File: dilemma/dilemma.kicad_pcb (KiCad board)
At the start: 2 copper layers, 142.3 x 95.1 mm, 72 parts, among them J1 S3B-PH-SM4-TB(LF)(SN), J2 Serial, J5 S3B-PH-SM4-TB(LF)(SN), SW1 SW_Push, SW10 SW_Push, SW11 SW_Push, SW12 SW_Push, SW13 SW_Push, SW14 SW_Push, SW15 SW_Push, SW16 SW_Push, SW17 SW_Push, SW2 SW_Push, SW26 SW_SPST, SW3 SW_Push, SW37 SW_SPST, SW4 SW_Push, SW5 SW_Push, SW6 SW_Push, SW7 SW_Push, SW8 SW_Push, SW9 SW_Push, U2 eliteC

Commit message: silkscreen
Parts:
- added G***: LOGO, LOGO, F.Cu at (140.1, 27.9)
- added G***: LOGO, LOGO, B.Cu at (140.1, 27.9)
- moved H1 11.8 mm to (131.1, 28.1)
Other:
- outline, holes or cut-outs redrawn

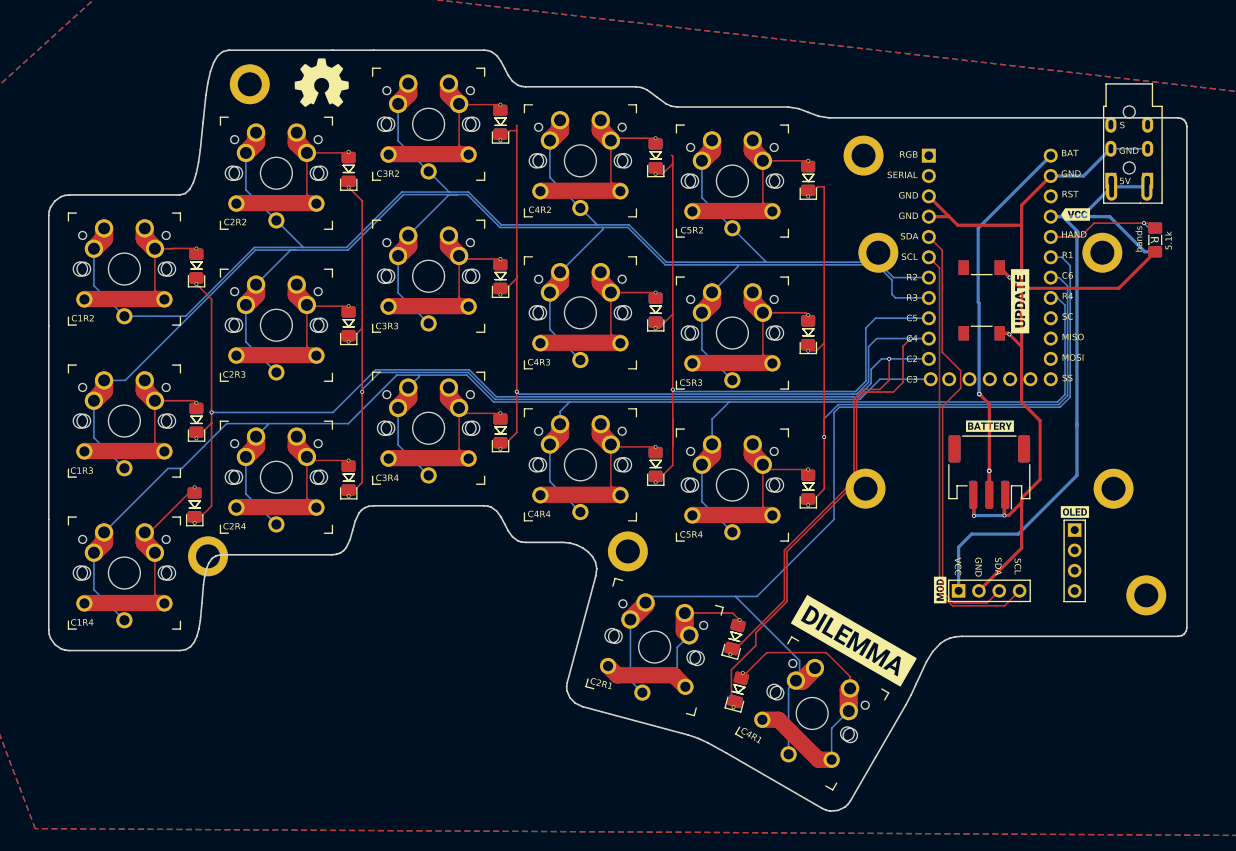
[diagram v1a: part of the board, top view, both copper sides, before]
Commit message: trackpad connector reversible
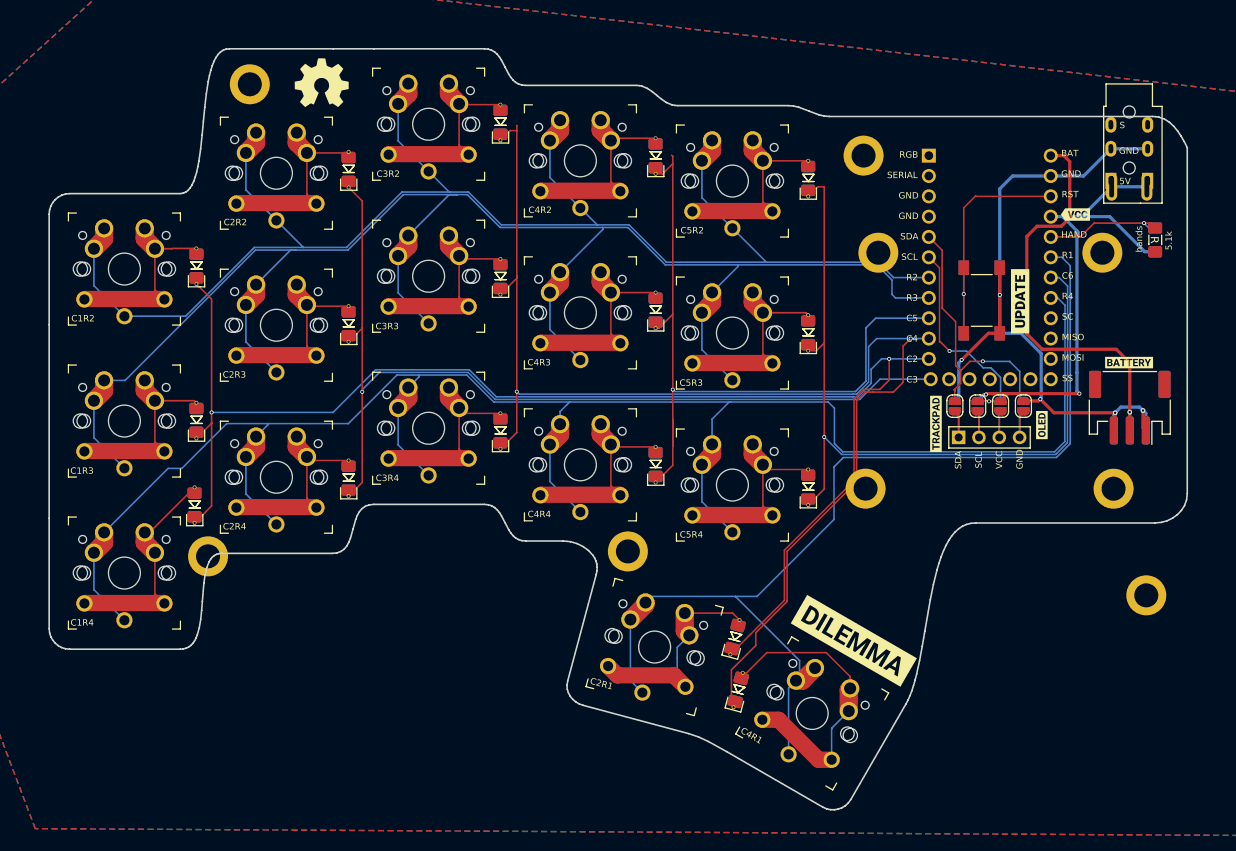
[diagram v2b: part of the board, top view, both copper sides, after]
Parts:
- removed O3: trackpad, footprints:PinHeader_1x04_P2.54mm_Vertical
- removed kibuzzard-628D3A32 (x2): G***, kibuzzard-628D3A32
- added JP1: Jumper_2_Open, footprints:SolderJumper-2_P1.3mm_Open_RoundedPad1.0x1.5mm, F.Cu at (219.2, 68.3)
- added JP2: Jumper_2_Open, footprints:SolderJumper-2_P1.3mm_Open_RoundedPad1.0x1.5mm, B.Cu at (227.8, 68.3)
- added JP3: Jumper_2_Open, footprints:SolderJumper-2_P1.3mm_Open_RoundedPad1.0x1.5mm, F.Cu at (222.1, 68.3)
- added JP4: Jumper_2_Open, footprints:SolderJumper-2_P1.3mm_Open_RoundedPad1.0x1.5mm, B.Cu at (224.9, 68.3)
- added JP5: Jumper_2_Open, footprints:SolderJumper-2_P1.3mm_Open_RoundedPad1.0x1.5mm, F.Cu at (224.9, 68.3)
- added JP6: Jumper_2_Open, footprints:SolderJumper-2_P1.3mm_Open_RoundedPad1.0x1.5mm, B.Cu at (222.1, 68.3)
- added JP7: Jumper_2_Open, footprints:SolderJumper-2_P1.3mm_Open_RoundedPad1.0x1.5mm, F.Cu at (227.8, 68.3)
- added JP8: Jumper_2_Open, footprints:SolderJumper-2_P1.3mm_Open_RoundedPad1.0x1.5mm, B.Cu at (219.2, 68.3)
- added kibuzzard-628E0199: G***, kibuzzard-628E0199, F.Cu at (216.9, 70.5)
- added kibuzzard-628E0199: G***, kibuzzard-628E0199, B.Cu at (216.9, 70.5)
- moved J5 19.3 mm to (241.1, 68.5)
- moved J1 19.3 mm to (241.1, 68.5)
- moved kibuzzard-628DFB5F 19.1 mm to (241.0, 62.9) (x2)
- moved O2 18.6 mm to (219.7, 72.2), turned to 90 degrees
- moved kibuzzard-628DFB48 11.6 mm to (230.1, 70.7), turned to -90 degrees
- moved kibuzzard-628DFB48 11.6 mm to (230.1, 70.7), turned to 90 degrees
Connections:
- O2 pad 1: sda_l -> Net-(O2-Pad1)
- O2 pad 2: scl_l -> Net-(O2-Pad2)
- O2 pad 3: Vcc_l -> Net-(O2-Pad3)
- O2 pad 4: Gnd_l -> Net-(O2-Pad4)
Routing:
- net Gnd_l: track 155.4 -> 118.5 mm, vias 4 -> 5
- net Rst_l: track 0.00 -> 35.7 mm, vias 0 -> 1
- net scl_l: track 53.9 -> 26.4 mm, vias 0 -> 2
- net sda_l: track 55.2 -> 34.8 mm, vias 0 -> 1
- net Vcc_l: track 81.8 -> 61.9 mm, vias 0 -> 2
- net row4_l: track 222.7 -> 233.9 mm
- net Net-(O2-Pad4): track 0.00 -> 6.92 mm
- net Net-(O2-Pad1): track 0.00 -> 6.92 mm
- net Net-(O2-Pad3): track 0.00 -> 6.65 mm
- net Net-(O2-Pad2): track 0.00 -> 6.65 mm
- net col5_l: track 131.2 -> 135.1 mm
- net bat_l: track 49.7 -> 53.3 mm, vias 2 -> 1
- net row1_l: track 130.2 -> 129.6 mm
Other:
- outline, holes or cut-outs redrawn

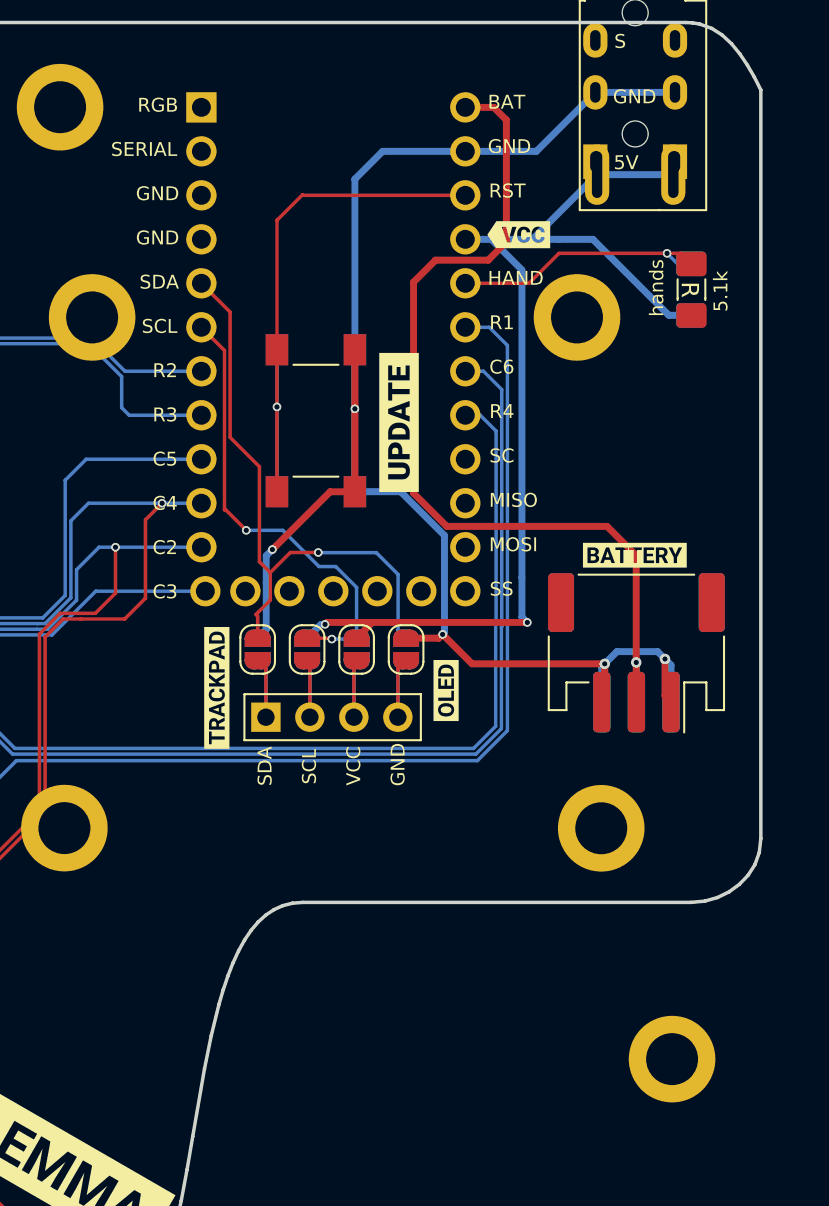
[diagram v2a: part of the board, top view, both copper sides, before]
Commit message: move battery connector and screw hole
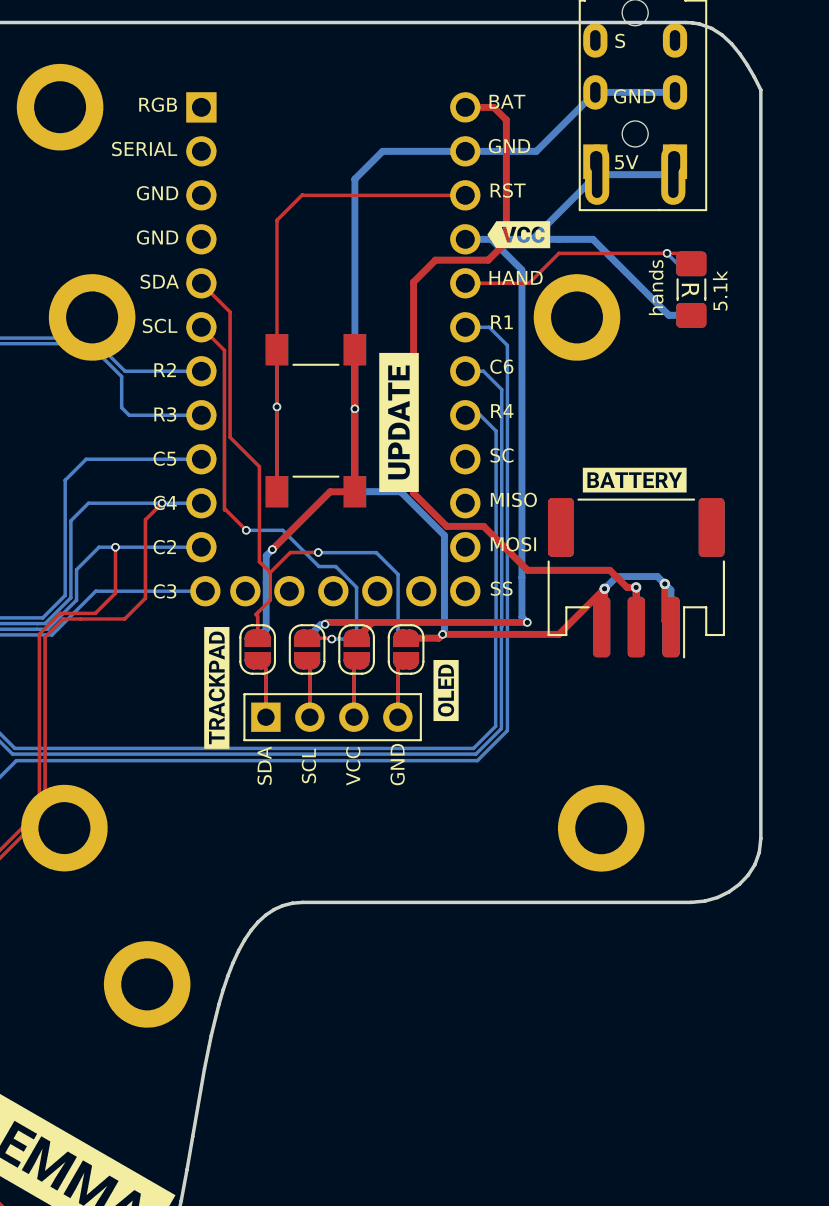
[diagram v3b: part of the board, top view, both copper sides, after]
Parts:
- moved H2 30.6 mm to (212.8, 87.7)
- moved kibuzzard-628DFB5F 4.33 mm to (241.0, 58.5) (x2)
- moved J1 4.33 mm to (241.1, 64.2)
- moved J5 4.33 mm to (241.1, 64.2)
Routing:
- net bat_l: track 53.3 -> 47.9 mm

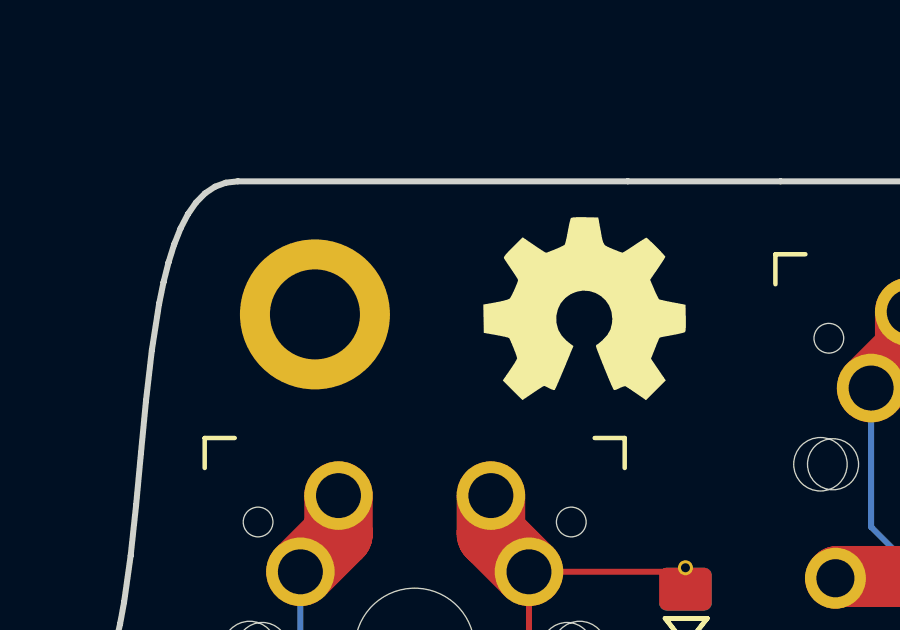
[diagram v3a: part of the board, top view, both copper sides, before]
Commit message: move cirque daughterboard to its own repo
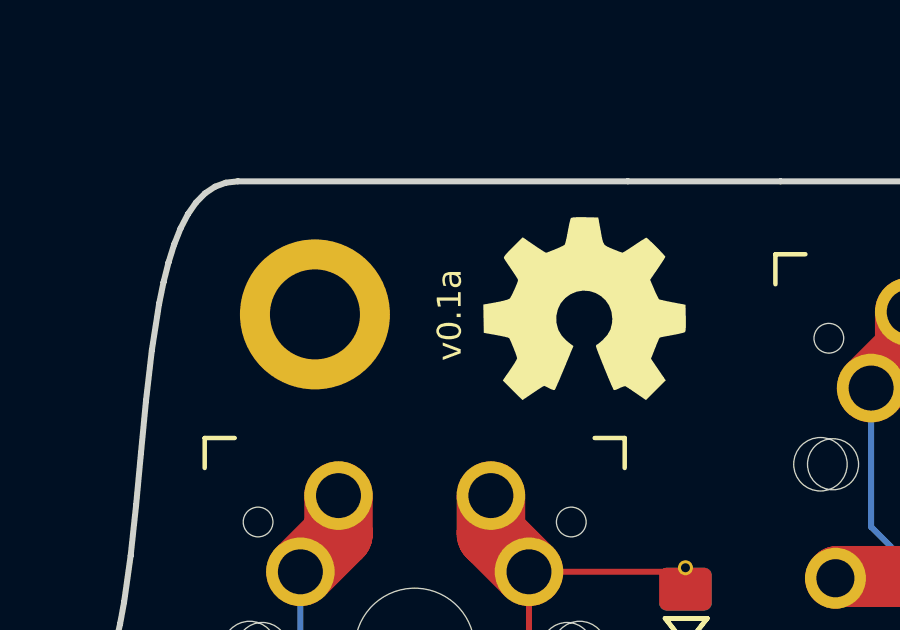
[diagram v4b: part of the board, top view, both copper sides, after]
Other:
- board text added: "v0.1a"
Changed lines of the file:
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@@
+    (effects (font (size 0.8 0.8) (thickness 0.12)))
+  )
+  (gr_text "v0.1a" (at 135.59 28.1 90) (layer "F.SilkS")
     (effects (font (size 0.8 0.8) (thickness 0.12)))
   )

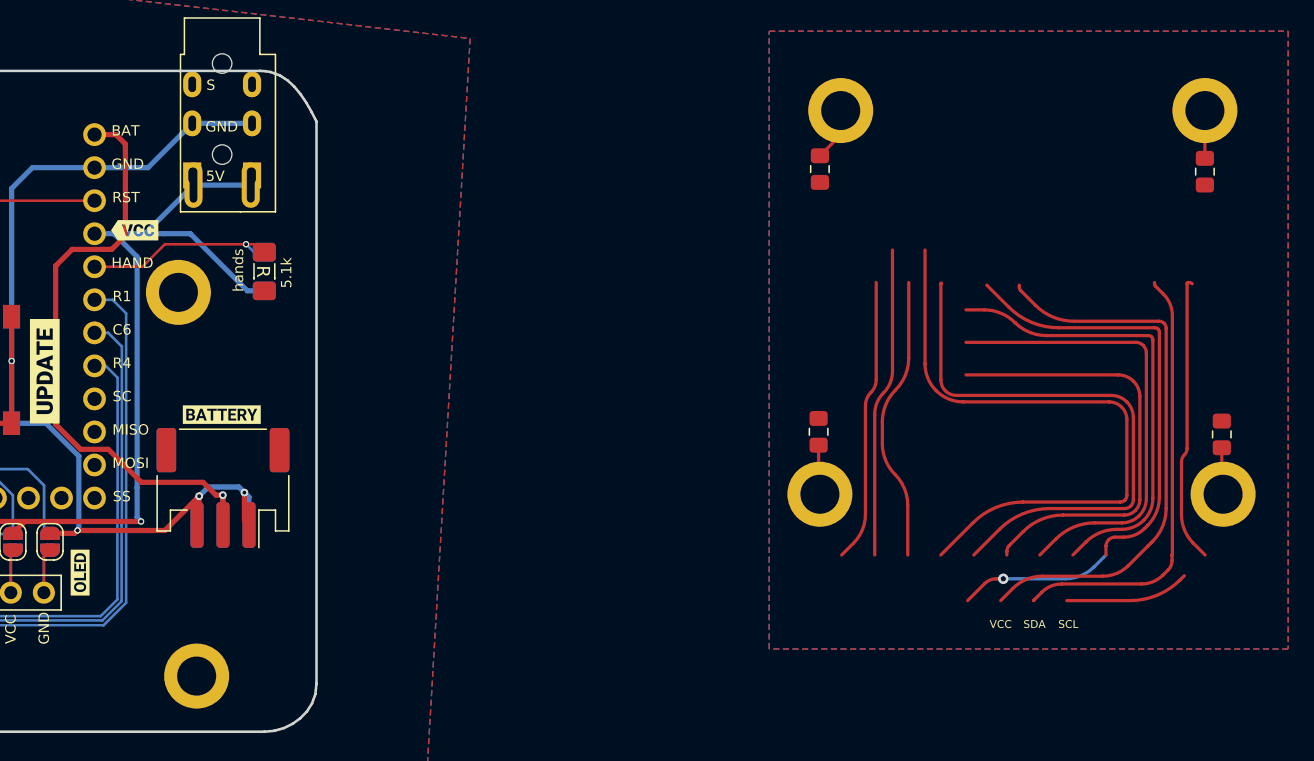
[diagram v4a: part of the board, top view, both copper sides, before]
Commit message: Added battery THT and the most common power switch used for wireless builds
Added battery THT and the most common power switch used for wireless builds
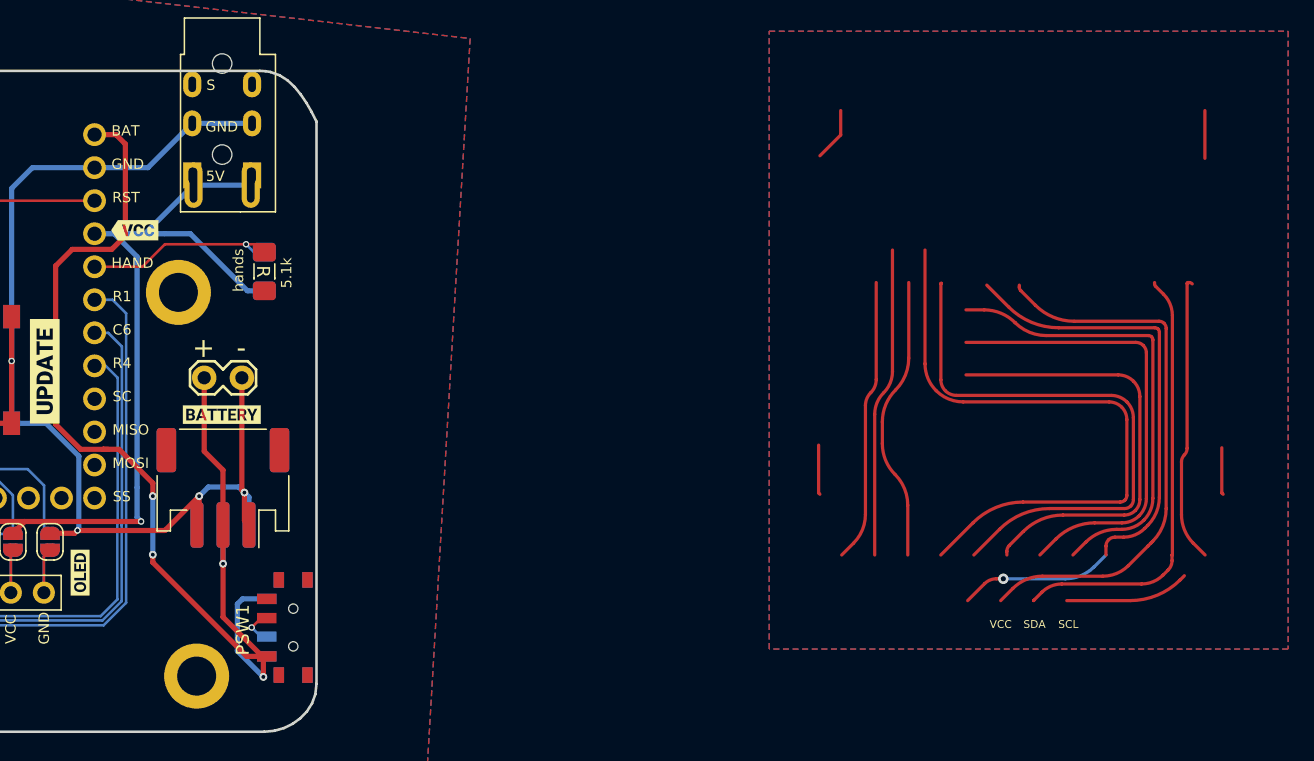
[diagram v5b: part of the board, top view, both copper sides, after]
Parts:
- removed FB1, FB2, FB3, FB4: FerriteBead, BK-CirqueDB:L_0805_2012Metric_Pad1.15x1.40mm_HandSolder
- removed H1000, H3000, H4000: M4, footprints:MountingHole_3mm_Pad_thin
- removed H20000 : M4, footprints:MountingHole_3mm_Pad_thin
- added J3: BATTERY_CONN_DEANS, Connectors:1X02_LOCK, F.Cu at (239.8, 55.7)
- added PSW1: SW_DPDT_x2, used_footprints:Switch_MSK-12C01-07, F.Cu at (246.5, 74.9)
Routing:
- net row3_l: track 0.00 -> 406.4 mm
- net row2_l: track 406.4 -> 0.00 mm
- net bat_l: track 47.9 -> 93.0 mm, vias 1 -> 4
- net Gnd_l: track 118.9 -> 130.7 mm, vias 5 -> 6
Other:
- board text added: "+"
- board text added: "-"
